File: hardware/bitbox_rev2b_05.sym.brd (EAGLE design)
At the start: 49.8 x 62.2 mm, 65 parts, among them IC3 LM317MSTT3, Q1 8MHz, U1 USD-SOCKETNEW, X2 2510-

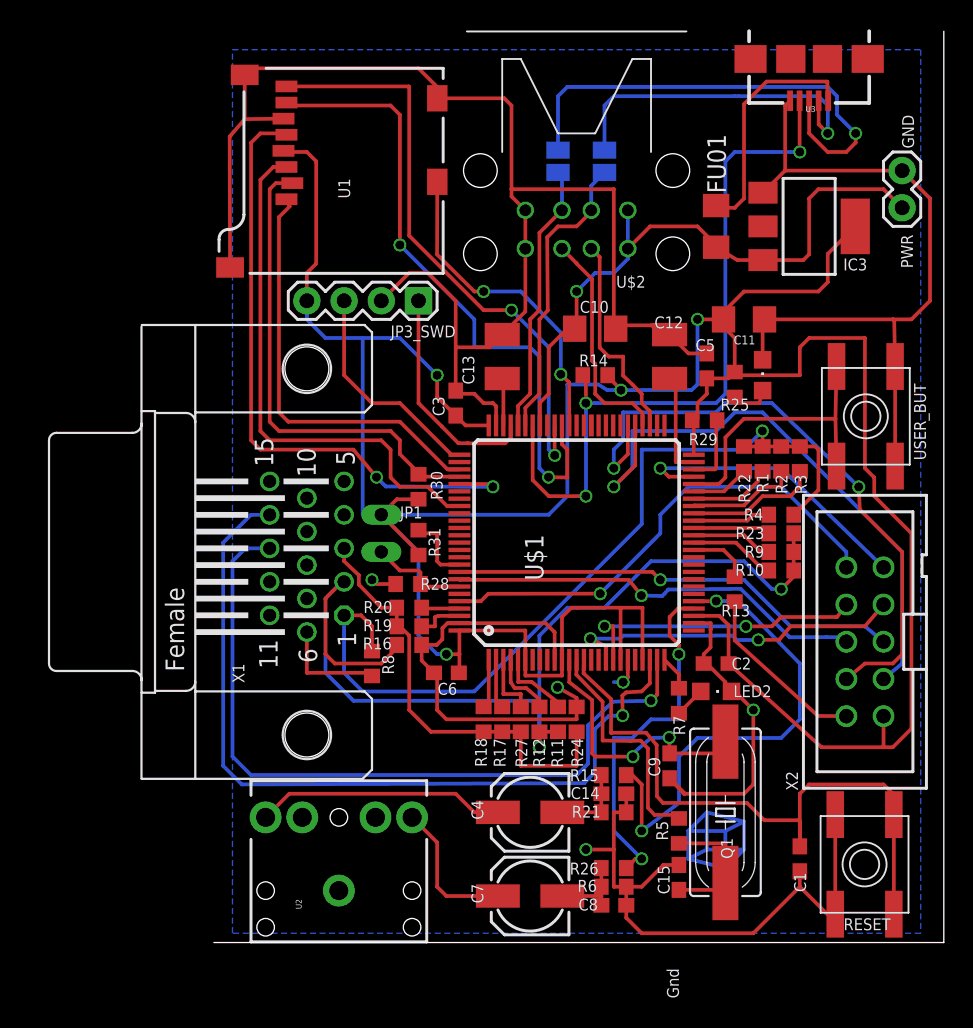
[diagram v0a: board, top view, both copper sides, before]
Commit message: updated hardware eagle files to version 2.5 (also called 2b)
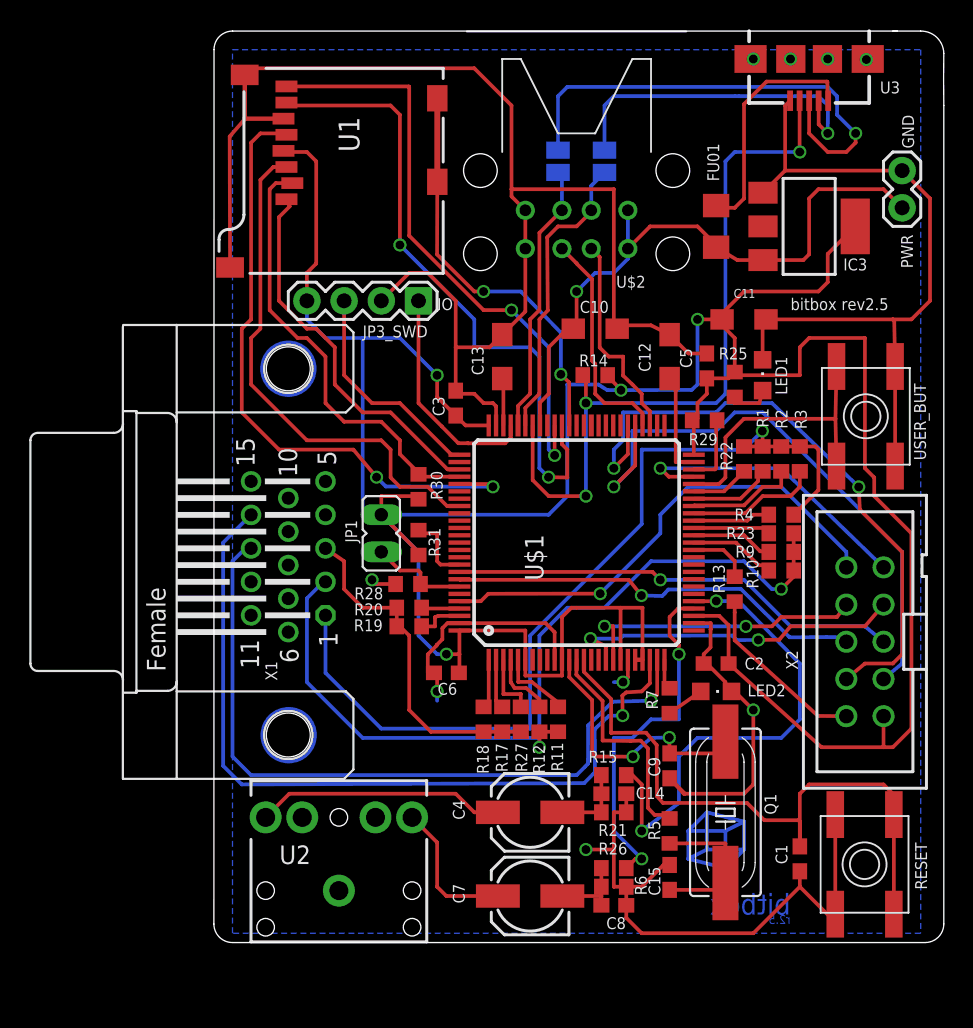
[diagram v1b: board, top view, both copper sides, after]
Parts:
- removed R16, R24, R8: 75r (unpopulated), resistor:R0603
- C10, C11: device resistor:C1206 -> resistor:SMC_A
- C12, C13: device resistor:SMC_B -> resistor:SMC_A
- R15, R26: value 500 -> 536r
- R21, R6: value 1k -> 1070r
- R25, R7: value 237 -> 220
- moved X1 1.27 mm to (21.0, 31.8)
- moved C15 0.63 mm to (47.0, 9.53)
- moved R5 0.63 mm to (47.0, 12.7)
- moved R7 0.63 mm to (47.0, 21.6)
- flipped JP1 to the top
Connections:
- net GND: now also C10.-, C11.-; no longer C10.2, C11.2, R16.1, R24.1, R8.1, U1.CD1
- net SDIO_SENSE: now also U1.CD1
- net VCC: now also C11.+, U$1.21; no longer C11.1
- net VGA_B: no longer R24.2
- net VGA_G: no longer R16.2
- net VGA_R: no longer R8.2
- net VIN: now also C10.+; no longer C10.1
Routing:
- net GND: track 264.8 -> 242.3 mm
- net VGA_G: track 70.2 -> 58.6 mm
- net VGA_B: track 30.3 -> 23.3 mm
- net SDIO_SENSE: track 22.2 -> 27.9 mm
- net VGA_R: track 58.7 -> 61.9 mm
- net SDIO_D2: track 29.0 -> 26.0 mm
- net SDIO_D3: track 33.0 -> 30.4 mm
- net VCC: track 216.8 -> 218.1 mm
- net VGA_V: track 55.8 -> 54.5 mm
- net VGA_H: track 51.9 -> 50.6 mm
- net N$6: track 9.52 -> 10.8 mm
- net SDIO_CMD: track 36.1 -> 35.2 mm
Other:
- outline, holes or cut-outs redrawn
- board text added: "IO"
- board text added: "IO GND CLK Vcc"
- board text added: "bitbox"
- board text added: "bitbox rev2.5"
- board text added: "r2.5"
- board text removed: "Gnd"
- board text removed: "bitbox rev2.06"
